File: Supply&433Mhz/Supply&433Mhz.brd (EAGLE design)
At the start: 65 x 56.5 mm, 17 parts, among them K1 61004021821, P1 DF11-06-2DSA, Q1 BS170

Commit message: Use SB1H100 as protection diode instead of SB160.
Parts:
- D3, D4: value SB160 -> SB1H100
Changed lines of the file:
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@@
 <attribute name="VALUE" x="21.5" y="35.95" size="1.27" layer="27" rot="R180" align="top-center"/>
 </element>
-<element name="D3" library="diode" package="DO41-7.6" value="SB160" x="9.1" y="23.5" smashed="yes" rot="R90">
+<element name="D3" library="diode" package="DO41-7.6" value="SB1H100" x="9.1" y="23.5" smashed="yes" rot="R90">
 <attribute name="NAME" x="7.85" y="23.5" size="1.27" layer="25" font="vector" ratio="10" rot="R90" align="bottom-center"/>
 <attribute name="VALUE" x="11.767" y="21.214" size="1.27" layer="27" ratio="10" rot="R90"/>
 </element>
-<element name="D4" library="diode" package="DO41-7.6" value="SB160" x="9.1" y="33.5" smashed="yes" rot="R270">
+<element name="D4" library="diode" package="DO41-7.6" value="SB1H100" x="9.1" y="33.5" smashed="yes" rot="R270">
 <attribute name="NAME" x="7.85" y="33.5" size="1.27" layer="25" font="vector" ratio="10" rot="R270" align="top-center"/>
 <attribute name="VALUE" x="6.433" y="35.786" size="1.27" layer="27" ratio="10" rot="R270"/>

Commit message: Use 1K as pull-up instead of 10K.
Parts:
- R1, R2: value 10K -> 1K
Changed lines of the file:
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@@
 <attribute name="NAME" x="46.79" y="42.2" size="1.27" layer="25" font="vector" ratio="10" rot="R90" align="top-left"/>
 </element>
-<element name="R2" library="rcl" package="0204V" value="10K" x="43.25" y="46.25" smashed="yes" rot="R180">
+<element name="R2" library="rcl" package="0204V" value="1K" x="43.25" y="46.25" smashed="yes" rot="R180">
 <attribute name="MPN" value="" x="43.25" y="52.25" size="1.778" layer="27" rot="R180" display="off"/>
 <attribute name="MF" value="" x="43.25" y="52.25" size="1.778" layer="27" rot="R180" display="off"/>
@@
 <attribute name="VALUE" x="45.3836" y="48.5614" size="1.27" layer="27" ratio="10" rot="R180"/>
 </element>
-<element name="R1" library="rcl" package="0204V" value="10K" x="44.65" y="38.39" smashed="yes" rot="R180">
+<element name="R1" library="rcl" package="0204V" value="1K" x="44.65" y="38.39" smashed="yes" rot="R180">
 <attribute name="MPN" value="" x="49.65" y="50.39" size="1.778" layer="27" rot="R180" display="off"/>
 <attribute name="MF" value="" x="49.65" y="50.39" size="1.778" layer="27" rot="R180" display="off"/>

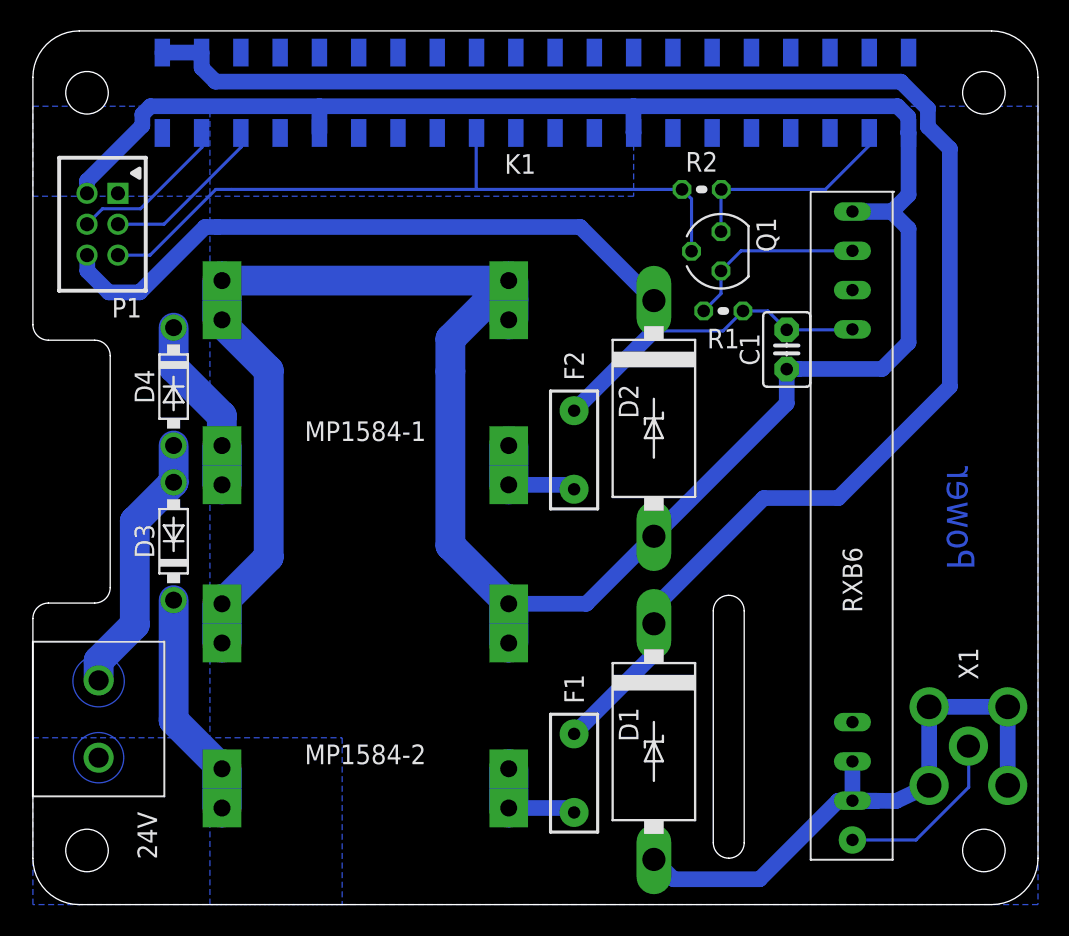
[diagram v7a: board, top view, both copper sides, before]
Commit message: Replace package for DF11 connector.
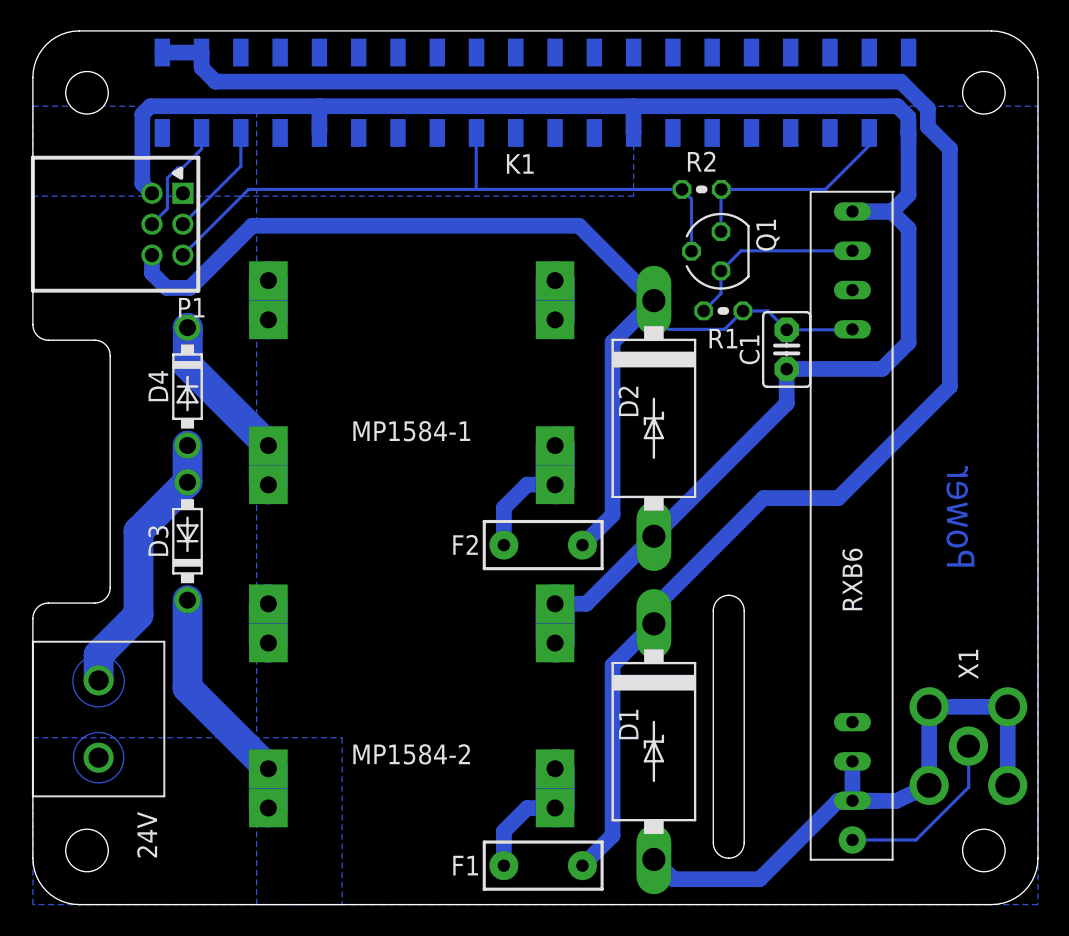
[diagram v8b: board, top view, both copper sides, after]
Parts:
- P1: value DF11-06-2DSA -> DF11-06-2DS; device con-hirose-df11:DF11-06DP-2DSA -> con-hirose-df11:DF11-06DP-2DS
- moved F2 6.47 mm to (33.0, 23.2), turned to 0 degrees
- moved F1 6.31 mm to (33.0, 2.52), turned to 180 degrees
- moved P1 4.20 mm to (8.70, 44.0)
- moved MP1584-1 3.00 mm to (24.5, 33.8)
- moved MP1584-2 3.00 mm to (24.5, 12.8)
- moved D3 0.90 mm to (10.0, 23.5)
- moved D4 0.90 mm to (10.0, 33.5)
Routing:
- net GND: track 228.5 -> 160.8 mm
- net N$5: track 105.5 -> 113.8 mm
- net N$2: track 65.1 -> 70.6 mm
- net N$11: track 46.3 -> 42.7 mm
- net N$1: track 11.0 -> 7.45 mm
- net N$12: track 10.4 -> 7.42 mm
- net N$6: track 6.89 -> 8.89 mm
- net N$4: track 6.89 -> 8.69 mm
- net N$9: track 11.5 -> 12.9 mm
- net N$7: track 14.8 -> 15.6 mm
